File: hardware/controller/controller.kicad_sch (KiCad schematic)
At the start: 4 parts, among them U1 ZX-PM2.54-1-16PY, U2 ZX-PM2.54-1-16PY, U3 ZX-PM2.54-1-16PY, U4 ZX-PM2.54-1-16PY

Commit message: feedback on the controller
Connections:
- net BACKUP1: now reaches U2.14
- net BACKUP1: now also U4.14
- net BACKUP2: now reaches U2.15
- net BACKUP2: now also U4.15
- net EYE_TO_EAR_FBK: now reaches U3.16
- net EYE_TO_EAR_FBK: now also U1.15
- net +3.3V: now reaches U4.5
- net +5V renamed +4V
- no-connect marks 33 -> 26
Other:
- note added: "i think you want this to sync up devices"

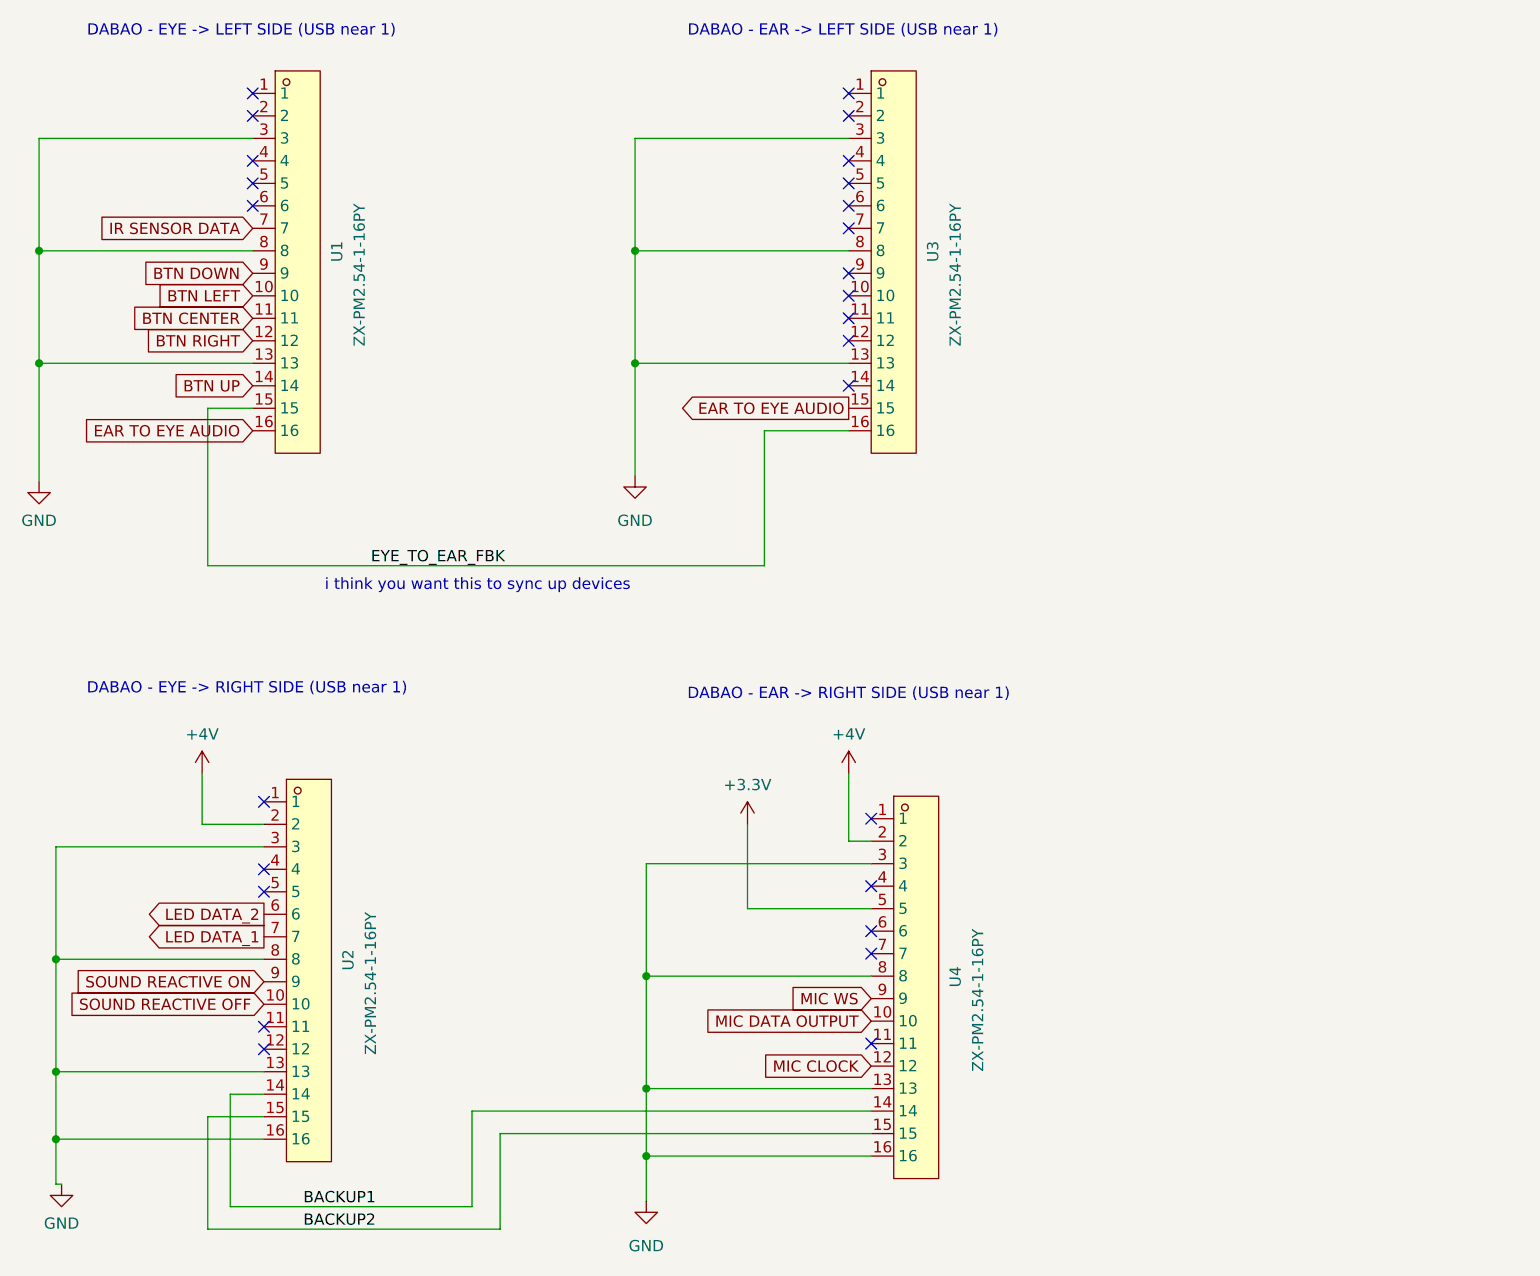
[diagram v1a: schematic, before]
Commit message: working on updating controller board
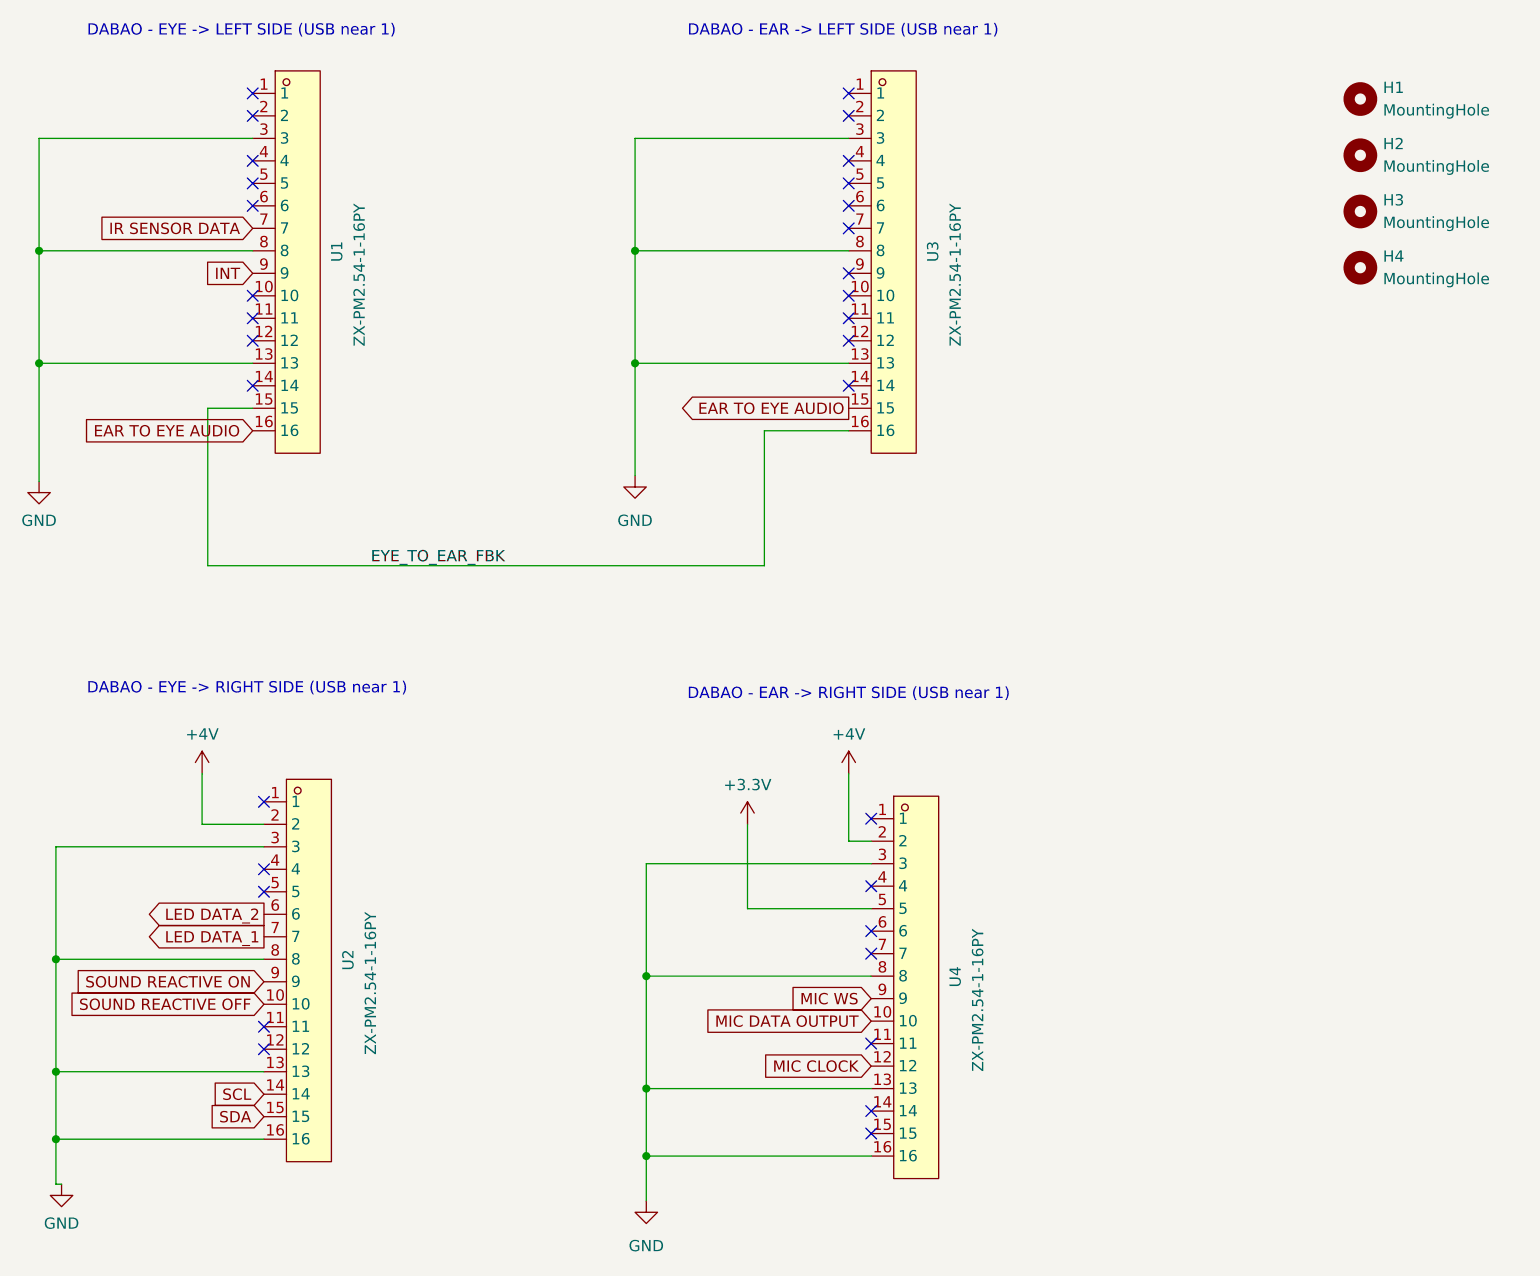
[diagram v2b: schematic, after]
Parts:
- added H1, H2, H3, H4: MountingHole, MountingHole:MountingHole_3.2mm_M3_Pad, symbol Mechanical:MountingHole
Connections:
- net BACKUP1: no longer names the net of U4.14
- net BACKUP1: no longer U2.14
- net BACKUP2: no longer names the net of U4.15
- net BACKUP2: no longer U2.15
- net BTN CENTER: no longer names the net of U1.11
- net BTN DOWN renamed INT
- net BTN LEFT: no longer names the net of U1.10
- net BTN RIGHT: no longer names the net of U1.12
- net BTN UP: no longer names the net of U1.14
- new net SCL: U2.14
- new net SDA: U2.15
- no-connect marks 26 -> 32
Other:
- note removed: "i think you want this to sync up devices"

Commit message: revised controller board
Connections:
- net +3.3V: now also U2.5
- no-connect marks 32 -> 31
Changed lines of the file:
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@@
-	)
-	(no_connect
-		(at 95.25 124.46)
 	)
 	(no_connect
@@
 	(wire
 		(pts
+			(xy 81.28 114.935) (xy 81.28 124.46)
+		)
+		(stroke
+			(width 0)
+			(type default)
+		)
+	)
+	(wire
+		(pts
 			(xy 151.765 72.39) (xy 151.765 87.63)
 		)
@@
 		(pts
 			(xy 161.29 118.745) (xy 161.29 111.125)
+		)
+		(stroke
+			(width 0)
+			(type default)
+		)
+	)
+	(wire
+		(pts
+			(xy 95.25 124.46) (xy 81.28 124.46)
 		)
 		(stroke
@@
 					(unit 1)
 				)
+			)
+		)
+	)
+	(symbol
+		(lib_id "power:+3.3V")
+		(at 81.28 114.935 0)
+		(unit 1)
+		(body_style 1)
+		(exclude_from_sim no)
+		(in_bom yes)
+		(on_board yes)
+		(in_pos_files yes)
+		(dnp no)
+		(fields_autoplaced yes)
+		(property "Reference" "#PWR056"
+			(at 81.28 118.745 0)
+			(hide yes)
+			(show_name no)
+			(do_not_autoplace no)
+			(effects
+				(font
+					(size 1.27 1.27)
+				)
+			)
+		)
+		(property "Value" "+3.3V"
+			(at 81.28 110.49 0)
+			(show_name no)
+			(do_not_autoplace no)
+			(effects
+				(font
+					(size 1.27 1.27)
+				)
+			)
+		)
+		(property "Footprint" ""
+			(at 81.28 114.935 0)
+			(hide yes)
+			(show_name no)
+			(do_not_autoplace no)
+			(effects
+				(font
+					(size 1.27 1.27)
+				)
+			)
+		)
+		(property "Datasheet" ""
+			(at 81.28 114.935 0)
+			(hide yes)
+			(show_name no)
+			(do_not_autoplace no)
+			(effects
+				(font
+					(size 1.27 1.27)
+				)
+			)
+		)
+		(property "Description" "Power symbol creates a global label with name \"+3.3V\""
+			(at 81.28 114.935 0)
+			(hide yes)
+			(show_name no)
+			(do_not_autoplace no)
+			(effects
+				(font
+					(size 1.27 1.27)
+				)
+			)
+		)
+		(pin "1"
+		)
+		(instances
+			(project "controller"
+				(path "/2ec1a6cc-e255-4c8d-bf32-cfafd13c2b2e"
+					(reference "#PWR056")
+					(unit 1)
+				)

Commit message: cleanup and prep for ordering
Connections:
- net SOUND REACTIVE OFF: no longer names the net of U2.10
- net SOUND REACTIVE ON: no longer names the net of U2.9
- no-connect marks 31 -> 33
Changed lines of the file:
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@@
+	)
+	(no_connect
+		(at 95.25 137.16)
 	)
 	(no_connect
@@
 	(no_connect
 		(at 161.29 57.15)
+	)
+	(no_connect
+		(at 95.25 134.62)
 	)
 	(no_connect
@@
 		)
 	)
-	(global_label "SOUND REACTIVE ON"
-		(shape input)
-		(at 95.25 134.62 180)
-		(fields_autoplaced yes)
-		(effects
-			(font
-				(size 1.27 1.27)
-			)
-			(justify right)
-		)
-		(property "Intersheetrefs" "${INTERSHEET_REFS}"
-			(at 72.61 134.62 0)
-			(hide yes)
-			(show_name no)
-			(do_not_autoplace no)
-			(effects
-				(font
-					(size 1.27 1.27)
-				)
-				(justify right)
-			)
-		)
-	)
 	(global_label "EAR TO EYE AUDIO"
 		(shape input)
@@
 			(hide yes)
 			(show_name no)
-			(do_not_autoplace no)
-			(effects
-				(font
-					(size 1.27 1.27)
-				)
-				(justify right)
-			)
-		)
-	)
-	(global_label "SOUND REACTIVE OFF"
-		(shape input)
-		(at 95.25 137.16 180)
-		(fields_autoplaced yes)
-		(effects
-			(font
-				(size 1.27 1.27)
-			)
-			(justify right)
-		)
-		(property "Intersheetrefs" "${INTERSHEET_REFS}"
-			(at 71.7633 137.16 0)
-			(hide yes)
-			(show_name no)
